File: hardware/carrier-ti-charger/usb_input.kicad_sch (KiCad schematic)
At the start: 8 parts, among them J1 MC-107DMS

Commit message: TI charger
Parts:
- added R65, R66: 5.1k 1%, Resistor_SMD:R_0603_1608Metric, symbol Device:R
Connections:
- net GND: now also R65.2, R66.2
- net USB_CC1: now also R65.1
- net USB_CC2: now also R66.1

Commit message: Align I2C resistors for 100kHZ ops.
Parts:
- C1: value 4.7u 50V X7R -> 4.7u 16V X5R; footprint Capacitor_SMD:C_0805_2012Metric -> Capacitor_SMD:C_0603_1608Metric; LCSC C437557 -> C19666
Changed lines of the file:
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@@
 			)
 		)
-		(property "Value" "4.7u 50V X7R"
+		(property "Value" "4.7u 16V X5R"
 			(at 101.6 62.23 0)
 			(show_name no)
@@
 			)
 		)
-		(property "Footprint" "Capacitor_SMD:C_0805_2012Metric"
+		(property "Footprint" "Capacitor_SMD:C_0603_1608Metric"
 			(at 99.06 60.96 0)
 			(hide yes)
@@
 			)
 		)
-		(property "LCSC" "C437557"
+		(property "LCSC" "C19666"
 			(at 99.06 60.96 0)
 			(hide yes)

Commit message: Other MH's.
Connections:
- net USB_DN renamed USB_D-
- net USB_DP renamed USB_D+
- net USB_VBUS renamed +VUSB
- net USB_VBUS_J1 renamed +VUSB_J1
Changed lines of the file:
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@@
 		)
 	)
-	(global_label "USB_DN"
+	(global_label "USB_D-"
 		(shape bidirectional)
 		(at 91.44 86.36 0)
@@
 		)
 	)
-	(global_label "USB_VBUS_J1"
+	(global_label "+VUSB_J1"
 		(shape input)
 		(at 76.2 53.34 180)
@@
 		)
 	)
-	(global_label "USB_DP"
+	(global_label "USB_D+"
 		(shape bidirectional)
 		(at 71.12 91.44 0)
@@
 	)
 	(symbol
-		(lib_id "carrier:USB_VBUS")
+		(lib_id "carrier:+VUSB")
 		(at 114.3 53.34 0)
 		(unit 1)
@@
 			)
 		)
-		(property "Value" "USB_VBUS"
+		(property "Value" "+VUSB"
 			(at 114.3 49.53 0)
 			(show_name no)
@@
 			)
 		)
-		(property "Description" "Power symbol creates a global label with name \"USB_VBUS\""
+		(property "Description" "Power symbol creates a global label with name \"+VUSB\""
 			(at 114.3 53.34 0)
 			(hide yes)

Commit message: Add USB current detection.
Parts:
- removed R65, R66: 5.1k 1%, Resistor_SMD:R_0603_1608Metric, symbol Device:R
- added C57: 100n 50V, Capacitor_SMD:C_0603_1608Metric, symbol Device:C
- added R79: 887k 1%, Resistor_SMD:R_0603_1608Metric, symbol Device:R
- added U15: TUSB320LIRWBR, carrier:X2QFN-12_L1.6-W1.6-P0.40-TL, symbol carrier:TUSB320LIRWBR
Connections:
- net +VUSB: now also R79.1
- net GND: now also C57.2, U15.10 (GND), U15.11 (EN_N), U15.3 (PORT), U15.5 (ADDR)
- net USB_CC1: now also U15.1 (CC1)
- net USB_CC2: now also U15.2 (CC2)
- new net +ESP_3V3: C57.1, U15.12 (VDD)
- new net I2C_SCL: U15.8 (SCL/OUT2)
- new net I2C_SDA: U15.7 (SDA/OUT1)
- new net U15_VBUS_DET: R79.2, U15.4 (VBUS_DET)
- no-connect marks 2 -> 4
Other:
- note added: "TUSB320L, Type-C sink, I2C 0x47. Polled, INT_N unused. Always-on +ESP_3V3. Unpowered: CC Rd (dead battery)."

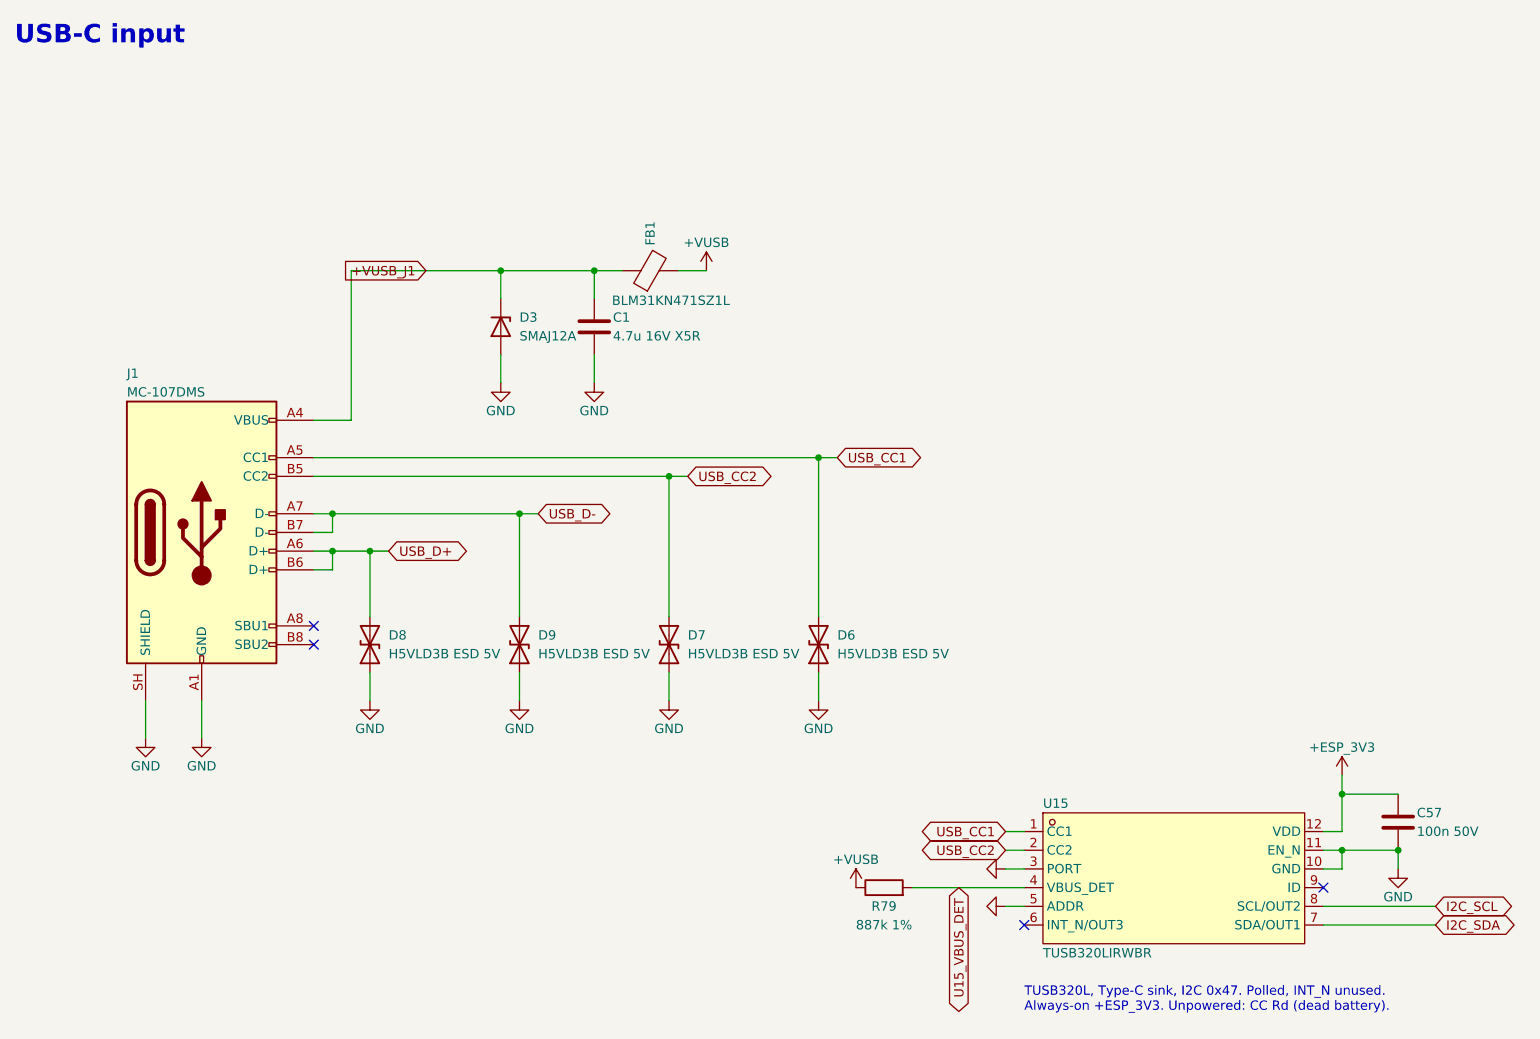
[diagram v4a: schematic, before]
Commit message: Switch to faster FUSB303B USB controller.
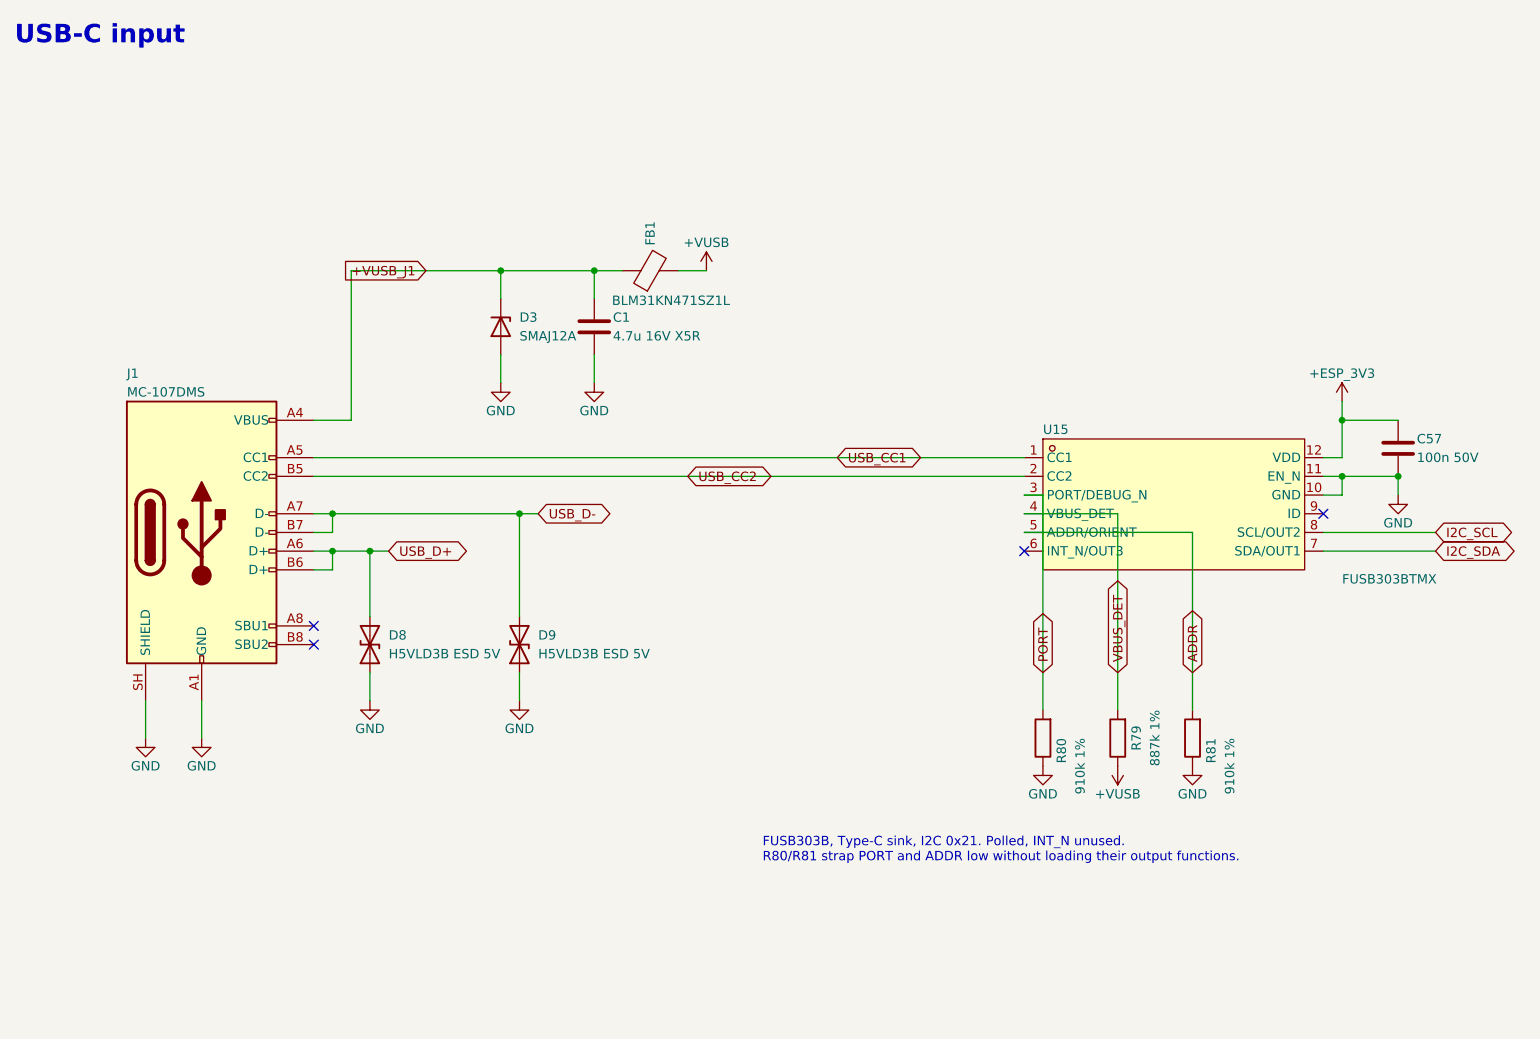
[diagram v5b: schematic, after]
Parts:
- removed D6, D7: H5VLD3B ESD 5V, Diode_SMD:D_SOD-323, symbol Device:D_TVS
- added R80, R81: 910k 1%, carrier:R_0402_1005Metric_NoSilk, symbol Device:R
- U15: value TUSB320LIRWBR -> FUSB303BTMX; symbol carrier:TUSB320LIRWBR -> carrier:FUSB303BTMX; LCSC C2836598 -> C895444
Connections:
- net GND: now also R80.1, R81.1; no longer U15.3 (PORT), U15.5 (ADDR)
- net U15_VBUS_DET renamed VBUS_DET
- new net ADDR: R81.2, U15.5 (ADDR/ORIENT)
- new net PORT: R80.2, U15.3 (PORT/DEBUG_N)
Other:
- note added: "FUSB303B, Type-C sink, I2C 0x21. Polled, INT_N unused. R80/R81 strap PORT and ADDR low without loading their output functions."
- note removed: "TUSB320L, Type-C sink, I2C 0x47. Polled, INT_N unused. Always-on +ESP_3V3. Unpowered: CC Rd (dead battery)."
- moved on the sheet: C57, R79, U15

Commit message: Fix missing parts.
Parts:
- R79: footprint Resistor_SMD:R_0603_1608Metric -> carrier:R_0402_1005Metric_NoSilk; LCSC C23259 -> C409935; MPN (none) -> ERJ2RKF8873X
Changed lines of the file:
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@@
 			)
 		)
-		(property "Footprint" "Resistor_SMD:R_0603_1608Metric"
+		(property "Footprint" "carrier:R_0402_1005Metric_NoSilk"
 			(at 170.18 116.84 0)
 			(hide yes)
@@
 			)
 		)
-		(property "LCSC" "C23259"
+		(property "LCSC" "C409935"
 			(at 170.18 116.84 0)
 			(hide yes)
+			(show_name no)
+			(do_not_autoplace no)
+			(effects
+				(font
+					(size 1.27 1.27)
+				)
+			)
+		)
+		(property "MPN" "ERJ2RKF8873X"
+			(at 170.18 116.84 0)
+			(hide yes)

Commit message: Consolidate bom.
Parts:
- C57: value 100n 50V -> 100n 16V; footprint Capacitor_SMD:C_0603_1608Metric -> carrier:C_0402_1005Metric_NoSilk; LCSC C14663 -> C1525; MPN (none) -> CL05B104KO5NNNC
- R79: value 887k 1% -> 1.5k 1%; LCSC C409935 -> C25867; MPN ERJ2RKF8873X -> 0402WGF1501TCE
- R80, R81: value 910k 1% -> 768k 1%; LCSC C25800 -> C49196905; MPN 0402WGF9103TCE -> FRC0402F7683TS
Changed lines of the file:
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@@
 			)
 		)
-		(property "Value" "910k 1%"
+		(property "Value" "768k 1%"
 			(at 185.42 116.84 90)
 			(show_name no)
@@
 			)
 		)
-		(property "Datasheet" "https://datasheet.lcsc.com/datasheet/pdf/0a975aaa49b7c97f38a963127be4a823.pdf?productCode=C25800"
+		(property "Datasheet" "https://www.lcsc.com/product-detail/C49196905.html"
 			(at 180.34 116.84 0)
 			(hide yes)
@@
 			)
 		)
-		(property "LCSC" "C25800"
+		(property "LCSC" "C49196905"
 			(at 180.34 116.84 0)
 			(hide yes)
@@
 			)
 		)
-		(property "MPN" "0402WGF9103TCE"
+		(property "MPN" "FRC0402F7683TS"
 			(at 180.34 116.84 0)
 			(hide yes)
@@
 			)
 		)
-		(property "Value" "910k 1%"
+		(property "Value" "768k 1%"
 			(at 165.1 116.84 90)
 			(show_name no)
@@
 			)
 		)
-		(property "Datasheet" "https://datasheet.lcsc.com/datasheet/pdf/0a975aaa49b7c97f38a963127be4a823.pdf?productCode=C25800"
+		(property "Datasheet" "https://www.lcsc.com/product-detail/C49196905.html"
 			(at 160.02 116.84 0)
 			(hide yes)
@@
 			)
 		)
-		(property "LCSC" "C25800"
+		(property "LCSC" "C49196905"
 			(at 160.02 116.84 0)
 			(hide yes)
@@
 			)
 		)
-		(property "MPN" "0402WGF9103TCE"
+		(property "MPN" "FRC0402F7683TS"
 			(at 160.02 116.84 0)
 			(hide yes)
@@
 			)
 		)
-		(property "Value" "100n 50V"
+		(property "Value" "100n 16V"
 			(at 210.82 78.74 0)
 			(show_name no)
@@
 			)
 		)
-		(property "Footprint" "Capacitor_SMD:C_0603_1608Metric"
+		(property "Footprint" "carrier:C_0402_1005Metric_NoSilk"
 			(at 208.28 77.47 0)
 			(hide yes)
@@
 			)
 		)
-		(property "LCSC" "C14663"
+		(property "LCSC" "C1525"
+			(at 208.28 77.47 0)
+			(hide yes)
+			(show_name no)
+			(do_not_autoplace no)
+			(effects
+				(font
+					(size 1.27 1.27)
+				)
+			)
+		)
+		(property "MPN" "CL05B104KO5NNNC"
 			(at 208.28 77.47 0)
 			(hide yes)
@@
 			)
 		)
-		(property "Value" "887k 1%"
+		(property "Value" "1.5k 1%"
 			(at 175.26 116.84 90)
 			(show_name no)
@@
 			)
 		)
-		(property "Description" "Resistor, VBUS_DET"
+		(property "Description" "VBUS_DET series resistor, surge current limit"
 			(at 170.18 116.84 0)
 			(hide yes)
@@
 			)
 		)
-		(property "LCSC" "C409935"
+		(property "LCSC" "C25867"
 			(at 170.18 116.84 0)
 			(hide yes)
@@
 			)
 		)
-		(property "MPN" "ERJ2RKF8873X"
+		(property "MPN" "0402WGF1501TCE"
 			(at 170.18 116.84 0)
 			(hide yes)
